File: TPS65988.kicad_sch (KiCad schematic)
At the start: 41 parts, among them J10 Conn_01x01, J11 USB_C_Receptacle, J12 Conn_01x03, J13 Conn_01x03, J14 Conn_01x05, J15 Conn_01x01, J9 USB_C_Receptacle, U13 TPD6S300A, U14 TPS65988, U15 TPD6S300A

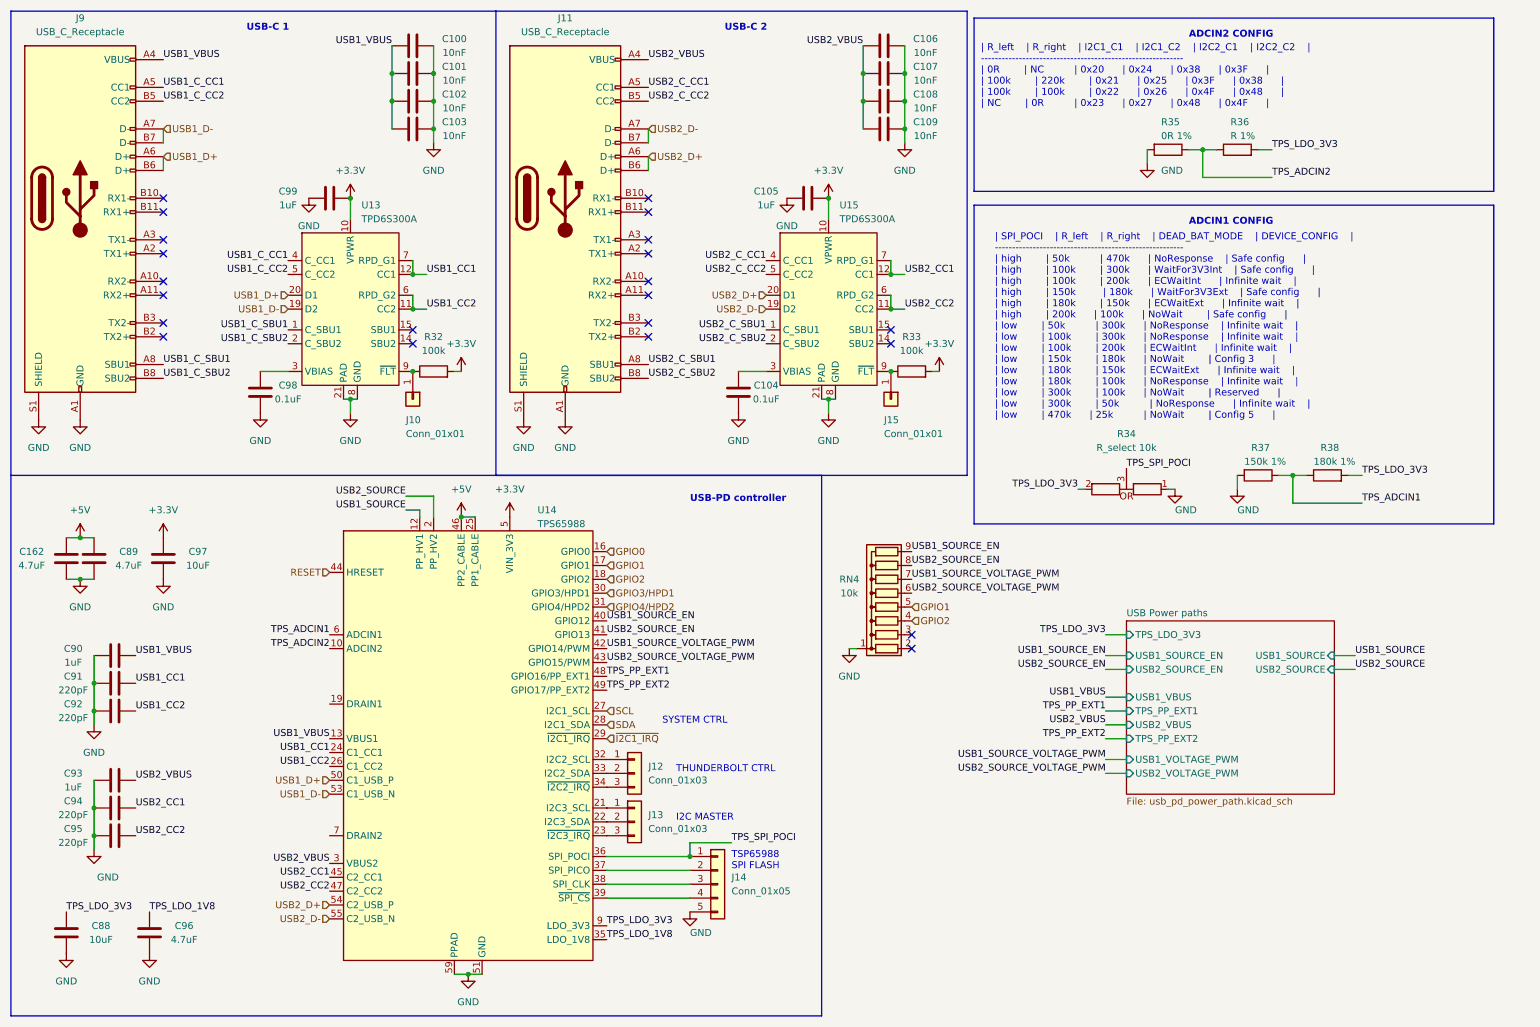
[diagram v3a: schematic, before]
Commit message: usb power source added, need to reassemble to 4-layers
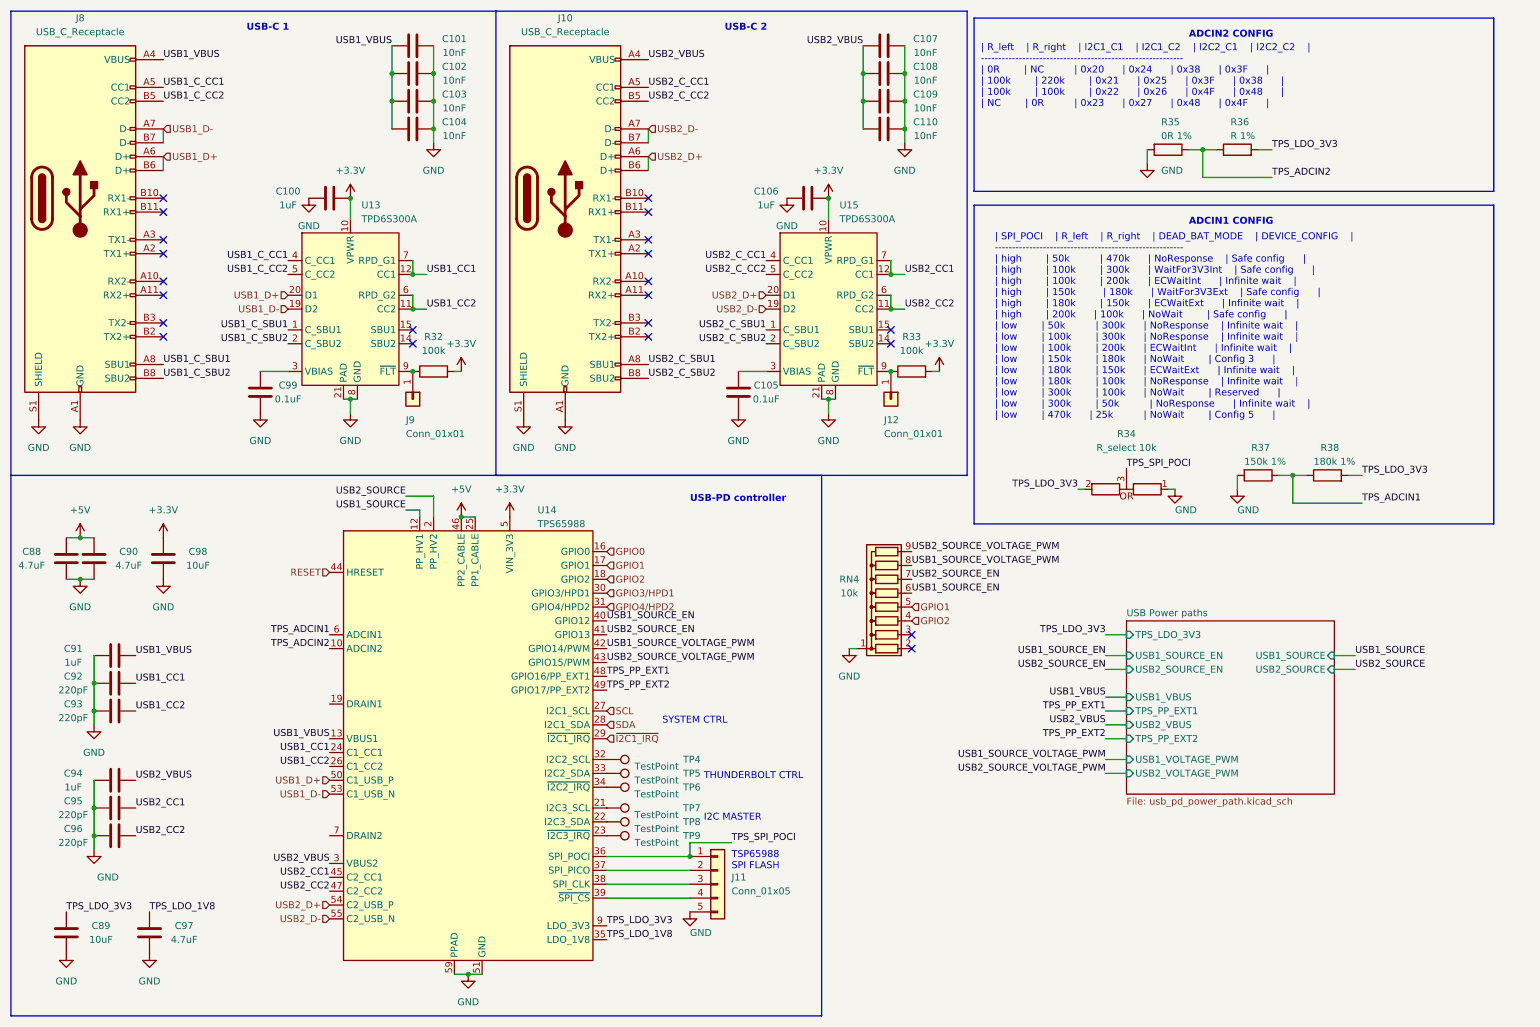
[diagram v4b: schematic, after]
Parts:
- removed J12, J13: Conn_01x03, Connector_PinSocket_2.54mm:PinSocket_1x03_P2.54mm_Vertical, symbol Connector_Generic:Conn_01x03
- added TP4, TP5, TP6, TP7, TP8, TP9: TestPoint, TestPoint:TestPoint_Pad_D1.5mm, symbol Connector:TestPoint
- renumbered C99 to C100, C100 to C101, C101 to C102, C102 to C103, C103 to C104, C104 to C105, C105 to C106, C106 to C107, C107 to C108, C108 to C109, C109 to C110, C162 to C88, C88 to C89, C89 to C90, C90 to C91, C91 to C92, C92 to C93, C93 to C94, C94 to C95, C95 to C96, C96 to C97, C97 to C98, C98 to C99, J11 to J10, J14 to J11, J15 to J12, J9 to J8, J10 to J9
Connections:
- net USB1_SOURCE_EN: now also RN4.6 (R5); no longer RN4.9 (R8)
- net USB1_SOURCE_VOLTAGE_PWM: now also RN4.8 (R7); no longer RN4.7 (R6)
- net USB2_SOURCE_EN: now also RN4.7 (R6); no longer RN4.8 (R7)
- net USB2_SOURCE_VOLTAGE_PWM: now also RN4.9 (R8); no longer RN4.6 (R5)
- net at U14.21 (I2C3_SCL): now also TP7.1
- net at U14.22 (I2C3_SDA): now also TP8.1
- net at U14.23 (~{I2C3_IRQ}): now also TP9.1
- net at U14.32 (I2C2_SCL): now also TP4.1
- net at U14.33 (I2C2_SDA): now also TP5.1
- net at U14.34 (~{I2C2_IRQ}): now also TP6.1

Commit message: done first iteration of pcb routing, slikscreen still broken
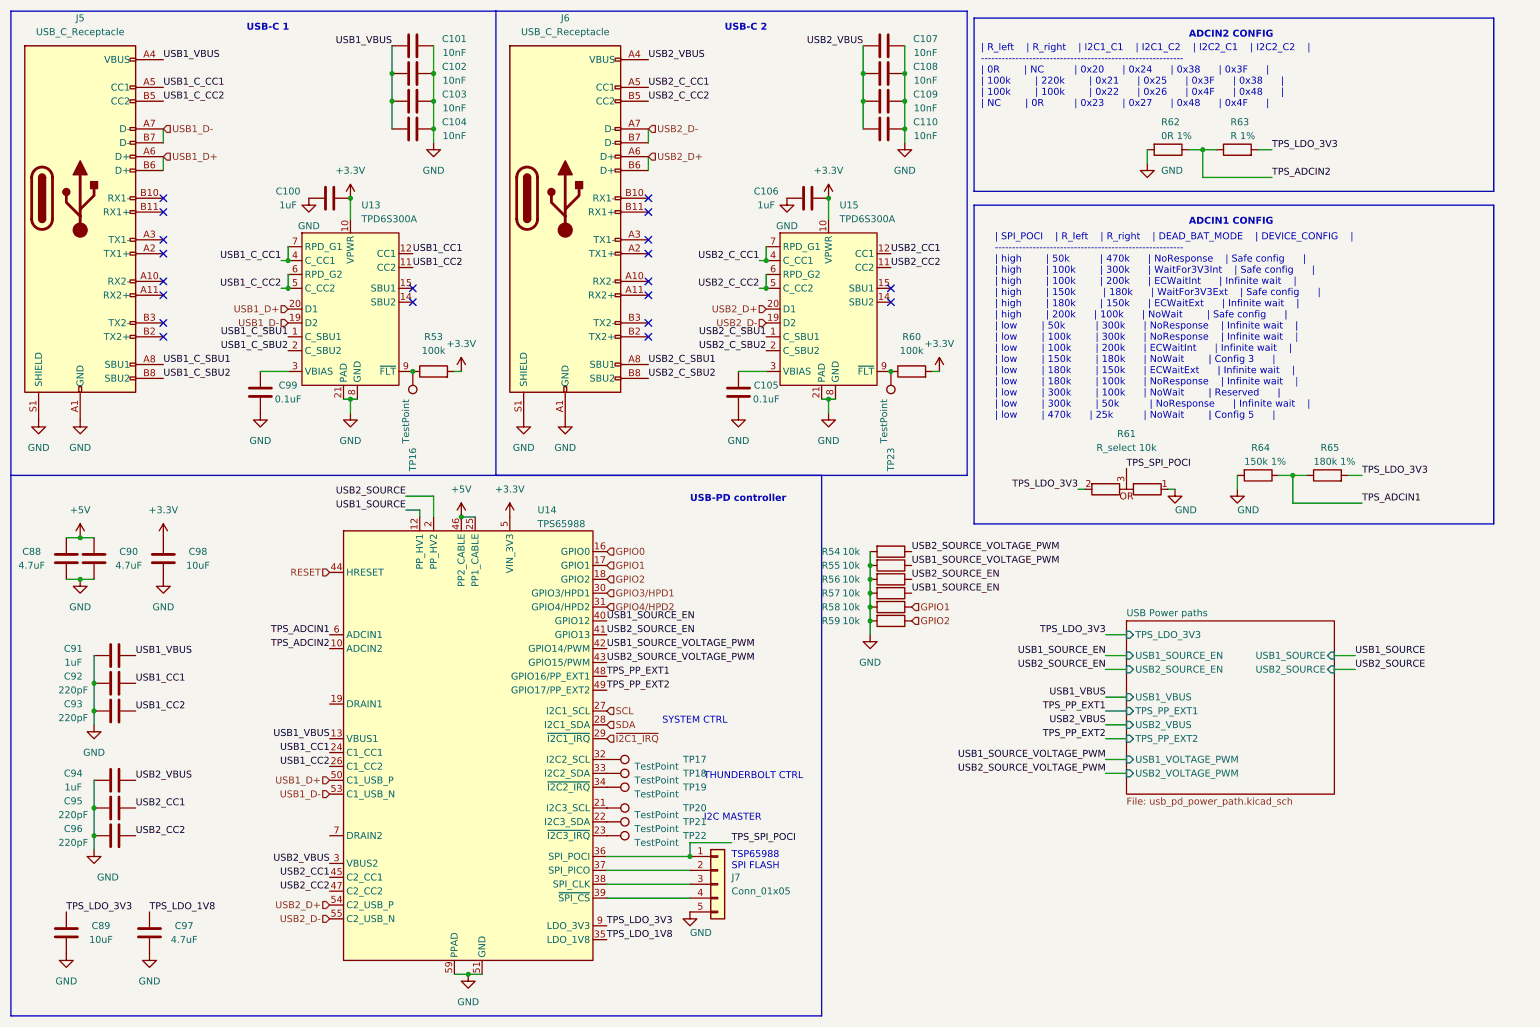
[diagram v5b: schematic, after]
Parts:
- removed J12, J9: Conn_01x01, Connector_PinSocket_2.54mm:PinSocket_1x01_P2.54mm_Vertical, symbol Connector_Generic:Conn_01x01
- removed RN4: 10k, Resistor_THT:R_Array_SIP9, symbol Device:R_Network08
- added R54, R55, R56, R57, R58, R59: 10k, Resistor_SMD:R_0603_1608Metric_Pad0.98x0.95mm_HandSolder, symbol Device:R
- added TP16, TP23: TestPoint, TestPoint:TestPoint_Pad_D1.5mm, symbol Connector:TestPoint
- renumbered J8 to J5, J10 to J6, J11 to J7, R32 to R53, R33 to R60, R34 to R61, R35 to R62, R36 to R63, R37 to R64, R38 to R65, TP4 to TP17, TP5 to TP18, TP6 to TP19, TP7 to TP20, TP8 to TP21, TP9 to TP22
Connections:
- net GND: now also R54.2, R55.2, R56.2, R57.2, R58.2, R59.2
- net GPIO1: now also R58.1
- net GPIO2: now also R59.1
- net USB1_CC1: no longer U13.7 (RPD_G1)
- net USB1_CC2: no longer U13.6 (RPD_G2)
- net USB1_C_CC1: now also U13.7 (RPD_G1)
- net USB1_C_CC2: now also U13.6 (RPD_G2)
- net USB1_SOURCE_EN: now also R57.1
- net USB1_SOURCE_VOLTAGE_PWM: now also R55.1
- net USB2_CC1: no longer U15.7 (RPD_G1)
- net USB2_CC2: no longer U15.6 (RPD_G2)
- net USB2_C_CC1: now also U15.7 (RPD_G1)
- net USB2_C_CC2: now also U15.6 (RPD_G2)
- net USB2_SOURCE_EN: now also R56.1
- net USB2_SOURCE_VOLTAGE_PWM: now also R54.1
- net at R60.1, U15.9 (~{FLT}): now also TP23.1
- net at R53.1, U13.9 (~{FLT}): now also TP16.1
- no-connect marks 22 -> 20

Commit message: mounting holes, fixes silkscreen
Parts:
- renumbered R53 to R52, R54 to R53, R55 to R54, R56 to R55, R57 to R56, R58 to R57, R59 to R58, R60 to R59, R61 to R60, R62 to R61, R63 to R62, R64 to R63, R65 to R64
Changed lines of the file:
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@@
   (symbol (lib_id "Device:R") (at 173.99 121.92 270) (unit 1)
     (in_bom yes) (on_board yes)
-    (property "Reference" "R58" (id 0) (at 161.29 121.92 90)
+    (property "Reference" "R57" (id 0) (at 161.29 121.92 90)
       (effects (font (size 1.27 1.27)) (justify left))
     )
@@
   (symbol (lib_id "Device:R") (at 173.99 114.3 270) (unit 1)
     (in_bom yes) (on_board yes)
-    (property "Reference" "R55" (id 0) (at 161.29 114.3 90)
+    (property "Reference" "R54" (id 0) (at 161.29 114.3 90)
       (effects (font (size 1.27 1.27)) (justify left))
     )
@@
   (symbol (lib_id "Device:R") (at 237.49 38.1 90) (unit 1)
     (in_bom yes) (on_board yes)
-    (property "Reference" "R63" (id 0) (at 236.22 33.02 90)
+    (property "Reference" "R62" (id 0) (at 236.22 33.02 90)
       (effects (font (size 1.27 1.27)) (justify right))
     )
@@
   (symbol (lib_id "Device:R") (at 177.8 78.74 90) (unit 1)
     (in_bom yes) (on_board yes) (fields_autoplaced)
-    (property "Reference" "R60" (id 0) (at 177.8 72.39 90))
+    (property "Reference" "R59" (id 0) (at 177.8 72.39 90))
     (property "Value" "100k" (id 1) (at 177.8 74.93 90))
     (property "Footprint" "Resistor_SMD:R_0603_1608Metric_Pad0.98x0.95mm_HandSolder" (id 2) (at 177.8 80.518 90)
@@
   (symbol (lib_id "airsoft_controller:R_select") (at 217.17 100.33 270) (unit 1)
     (in_bom yes) (on_board yes)
-    (property "Reference" "R61" (id 0) (at 217.17 90.17 90))
+    (property "Reference" "R60" (id 0) (at 217.17 90.17 90))
     (property "Value" "R_select 10k" (id 1) (at 217.17 92.71 90))
     (property "Footprint" "airsoft_controller:0603-R-select" (id 2) (at 217.17 100.33 0)
@@
   (symbol (lib_id "Device:R") (at 241.3 97.79 270) (unit 1)
     (in_bom yes) (on_board yes)
-    (property "Reference" "R64" (id 0) (at 240.03 92.71 90)
+    (property "Reference" "R63" (id 0) (at 240.03 92.71 90)
       (effects (font (size 1.27 1.27)) (justify left))
     )
@@
   (symbol (lib_id "Device:R") (at 173.99 124.46 270) (unit 1)
     (in_bom yes) (on_board yes)
-    (property "Reference" "R59" (id 0) (at 161.29 124.46 90)
+    (property "Reference" "R58" (id 0) (at 161.29 124.46 90)
       (effects (font (size 1.27 1.27)) (justify left))
     )
@@
   (symbol (lib_id "Device:R") (at 173.99 119.38 270) (unit 1)
     (in_bom yes) (on_board yes)
-    (property "Reference" "R57" (id 0) (at 161.29 119.38 90)
+    (property "Reference" "R56" (id 0) (at 161.29 119.38 90)
       (effects (font (size 1.27 1.27)) (justify left))
     )
@@
   (symbol (lib_id "Device:R") (at 254 97.79 90) (unit 1)
     (in_bom yes) (on_board yes)
-    (property "Reference" "R65" (id 0) (at 252.73 92.71 90)
+    (property "Reference" "R64" (id 0) (at 252.73 92.71 90)
       (effects (font (size 1.27 1.27)) (justify right))
     )
@@
   (symbol (lib_id "Device:R") (at 224.79 38.1 270) (unit 1)
     (in_bom yes) (on_board yes)
-    (property "Reference" "R62" (id 0) (at 223.52 33.02 90)
+    (property "Reference" "R61" (id 0) (at 223.52 33.02 90)
       (effects (font (size 1.27 1.27)) (justify left))
     )
@@
   (symbol (lib_id "Device:R") (at 90.17 78.74 90) (unit 1)
     (in_bom yes) (on_board yes) (fields_autoplaced)
-    (property "Reference" "R53" (id 0) (at 90.17 72.39 90))
+    (property "Reference" "R52" (id 0) (at 90.17 72.39 90))
     (property "Value" "100k" (id 1) (at 90.17 74.93 90))
     (property "Footprint" "Resistor_SMD:R_0603_1608Metric_Pad0.98x0.95mm_HandSolder" (id 2) (at 90.17 80.518 90)
@@
   (symbol (lib_id "Device:R") (at 173.99 111.76 270) (unit 1)
     (in_bom yes) (on_board yes)
-    (property "Reference" "R54" (id 0) (at 161.29 111.76 90)
+    (property "Reference" "R53" (id 0) (at 161.29 111.76 90)
       (effects (font (size 1.27 1.27)) (justify left))
     )
@@
   (symbol (lib_id "Device:R") (at 173.99 116.84 270) (unit 1)
     (in_bom yes) (on_board yes)
-    (property "Reference" "R56" (id 0) (at 161.29 116.84 90)
-      (effects (font (size 1.27 1.27)) (justify left))
-    )
+    (property "Reference" "R55" (id 0) (at 161.29 116.84 90)
+      (effects (font (size 1.27 1.27)) (justify left))
+    )
